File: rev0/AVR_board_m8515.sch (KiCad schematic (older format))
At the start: 19 parts, among them IC1 ATMEGA8515-A, IC2 ATMEGA8515-M, K1 SERIAL, P1 FTDI_HEADER, P2 LEFT_HEADER, P3 CONN_3X2, P4 RIGHT_HEADER, SW1 SW_PUSH, X1 CRYSTAL_TH, X2 CRYSTAL_SMD

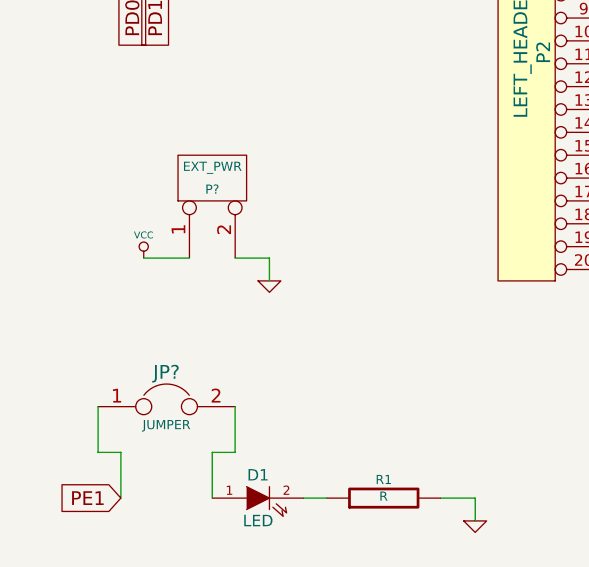
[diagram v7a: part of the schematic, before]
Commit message: fixed GND disconnects, will try to thicken the traces
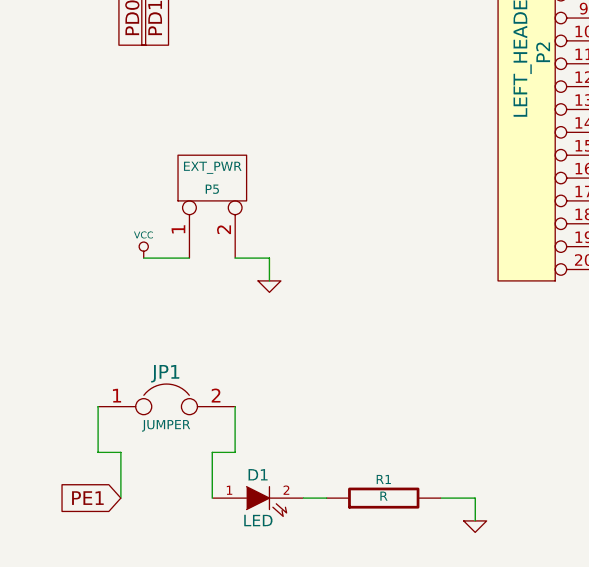
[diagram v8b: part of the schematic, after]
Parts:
- gave numbers to parts that had none: 2
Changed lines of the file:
@@
 $EndComp
 $Comp
-L GND #PWR01
+L GND #PWR8
 U 1 1 54186B5E
 P 4500 7050
-F 0 "#PWR01" H 4500 7050 30  0001 C CNN
+F 0 "#PWR8" H 4500 7050 30  0001 C CNN
 F 1 "GND" H 4500 6980 30  0001 C CNN
 F 2 "" H 4500 7050 60  0000 C CNN
@@
 $EndComp
 $Comp
-L GND #PWR02
+L GND #PWR7
 U 1 1 54186C19
 P 3500 5800
-F 0 "#PWR02" H 3500 5800 30  0001 C CNN
+F 0 "#PWR7" H 3500 5800 30  0001 C CNN
 F 1 "GND" H 3500 5730 30  0001 C CNN
 F 2 "" H 3500 5800 60  0000 C CNN
@@
 $EndComp
 $Comp
-L VCC #PWR03
+L VCC #PWR6
 U 1 1 54186C37
 P 3500 5050
-F 0 "#PWR03" H 3500 5150 30  0001 C CNN
+F 0 "#PWR6" H 3500 5150 30  0001 C CNN
 F 1 "VCC" H 3500 5150 30  0000 C CNN
 F 2 "" H 3500 5050 60  0000 C CNN
@@
 	3500 5300 3650 5300
 $Comp
-L GND #PWR04
+L GND #PWR12
 U 1 1 54186C8C
 P 7750 5500
-F 0 "#PWR04" H 7750 5500 30  0001 C CNN
+F 0 "#PWR12" H 7750 5500 30  0001 C CNN
 F 1 "GND" H 7750 5430 30  0001 C CNN
 F 2 "" H 7750 5500 60  0000 C CNN
@@
 	7350 3850 7350 3950
 $Comp
-L VCC #PWR05
+L VCC #PWR11
 U 1 1 54189251
 P 6600 800
-F 0 "#PWR05" H 6600 900 30  0001 C CNN
+F 0 "#PWR11" H 6600 900 30  0001 C CNN
 F 1 "VCC" H 6600 900 30  0000 C CNN
 F 2 "" H 6600 800 60  0000 C CNN
@@
 $EndComp
 $Comp
-L GND #PWR06
+L GND #PWR14
 U 1 1 5418A680
 P 10000 1250
-F 0 "#PWR06" H 10000 1250 30  0001 C CNN
+F 0 "#PWR14" H 10000 1250 30  0001 C CNN
 F 1 "GND" H 10000 1180 30  0001 C CNN
 F 2 "" H 10000 1250 60  0000 C CNN
@@
 PA0
 $Comp
-L VCC #PWR07
+L VCC #PWR13
 U 1 1 5418A7C7
 P 9950 5300
-F 0 "#PWR07" H 9950 5400 30  0001 C CNN
+F 0 "#PWR13" H 9950 5400 30  0001 C CNN
 F 1 "VCC" H 9950 5400 30  0000 C CNN
 F 2 "" H 9950 5300 60  0000 C CNN
@@
 $EndComp
 $Comp
-L VCC #PWR08
+L VCC #PWR10
 U 1 1 5418C02E
 P 5650 1500
-F 0 "#PWR08" H 5650 1600 30  0001 C CNN
+F 0 "#PWR10" H 5650 1600 30  0001 C CNN
 F 1 "VCC" H 5650 1600 30  0000 C CNN
 F 2 "" H 5650 1500 60  0000 C CNN
@@
 PB5
 $Comp
-L GND #PWR09
+L GND #PWR9
 U 1 1 5418C0DE
 P 5600 1950
-F 0 "#PWR09" H 5600 1950 30  0001 C CNN
+F 0 "#PWR9" H 5600 1950 30  0001 C CNN
 F 1 "GND" H 5600 1880 30  0001 C CNN
 F 2 "" H 5600 1950 60  0000 C CNN
@@
 	2250 3900 2350 3900
 $Comp
-L GND #PWR010
+L GND #PWR5
 U 1 1 5418F076
 P 3000 4000
-F 0 "#PWR010" H 3000 4000 30  0001 C CNN
+F 0 "#PWR5" H 3000 4000 30  0001 C CNN
 F 1 "GND" H 3000 3930 30  0001 C CNN
 F 2 "" H 3000 4000 60  0000 C CNN
@@
 $EndComp
 $Comp
-L GND #PWR011
+L GND #PWR1
 U 1 1 5418F501
 P 1050 1450
-F 0 "#PWR011" H 1050 1450 30  0001 C CNN
+F 0 "#PWR1" H 1050 1450 30  0001 C CNN
 F 1 "GND" H 1050 1380 30  0001 C CNN
 F 2 "" H 1050 1450 60  0000 C CNN
@@
 	1050 1350 1050 1450
 $Comp
-L VCC #PWR012
+L VCC #PWR2
 U 1 1 5418F6CA
 P 1400 1500
-F 0 "#PWR012" H 1400 1600 30  0001 C CNN
+F 0 "#PWR2" H 1400 1600 30  0001 C CNN
 F 1 "VCC" H 1400 1600 30  0000 C CNN
 F 2 "" H 1400 1500 60  0000 C CNN
@@
 Connection ~ 1150 1350
 $Comp
-L CONN_2 P?
+L CONN_2 P5
 U 1 1 54190E9B
 P 1850 2500
-F 0 "P?" V 1800 2500 40  0000 C CNN
+F 0 "P5" V 1800 2500 40  0000 C CNN
 F 1 "EXT_PWR" V 1900 2500 40  0000 C CNN
 F 2 "" H 1850 2500 60  0000 C CNN
@@
 $EndComp
 $Comp
-L VCC #PWR?
+L VCC #PWR3
 U 1 1 54190EB4
 P 1550 2850
-F 0 "#PWR?" H 1550 2950 30  0001 C CNN
+F 0 "#PWR3" H 1550 2950 30  0001 C CNN
 F 1 "VCC" H 1550 2950 30  0000 C CNN
 F 2 "" H 1550 2850 60  0000 C CNN
@@
 $EndComp
 $Comp
-L GND #PWR?
+L GND #PWR4
 U 1 1 54190EC3
 P 2100 2950
-F 0 "#PWR?" H 2100 2950 30  0001 C CNN
+F 0 "#PWR4" H 2100 2950 30  0001 C CNN
 F 1 "GND" H 2100 2880 30  0001 C CNN
 F 2 "" H 2100 2950 60  0000 C CNN
@@
 	1750 2850 1550 2850
 $Comp
-L JUMPER JP?
+L JUMPER JP1
 U 1 1 54191199
 P 1650 3500
-F 0 "JP?" H 1650 3650 60  0000 C CNN
+F 0 "JP1" H 1650 3650 60  0000 C CNN
 F 1 "JUMPER" H 1650 3420 40  0000 C CNN
 F 2 "" H 1650 3500 60  0000 C CNN
